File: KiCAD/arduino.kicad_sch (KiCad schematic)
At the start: 2 parts, among them U1 Si5351A_Breakout, U2 Metro_ESP32S3

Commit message: Work in Progress
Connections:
- net 3V3: now reaches U2.3V3_L (3V3)
- net 3V3: now also U1.VIN
- net SDA: now reaches U2.A4 (A4/SDA)
- net SDA: now also U1.SDA
- net SCL: now reaches U2.A5 (A5/SCL)
- net SCL: now also U1.SCL
- net GND: now reaches U2.GND_L (GND)
- net GND: now also U1.GND
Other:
- note added: "I2C pull-ups provided by Si5351A breakout (10 kΩ to 3.3 V). No additional pull-ups needed."

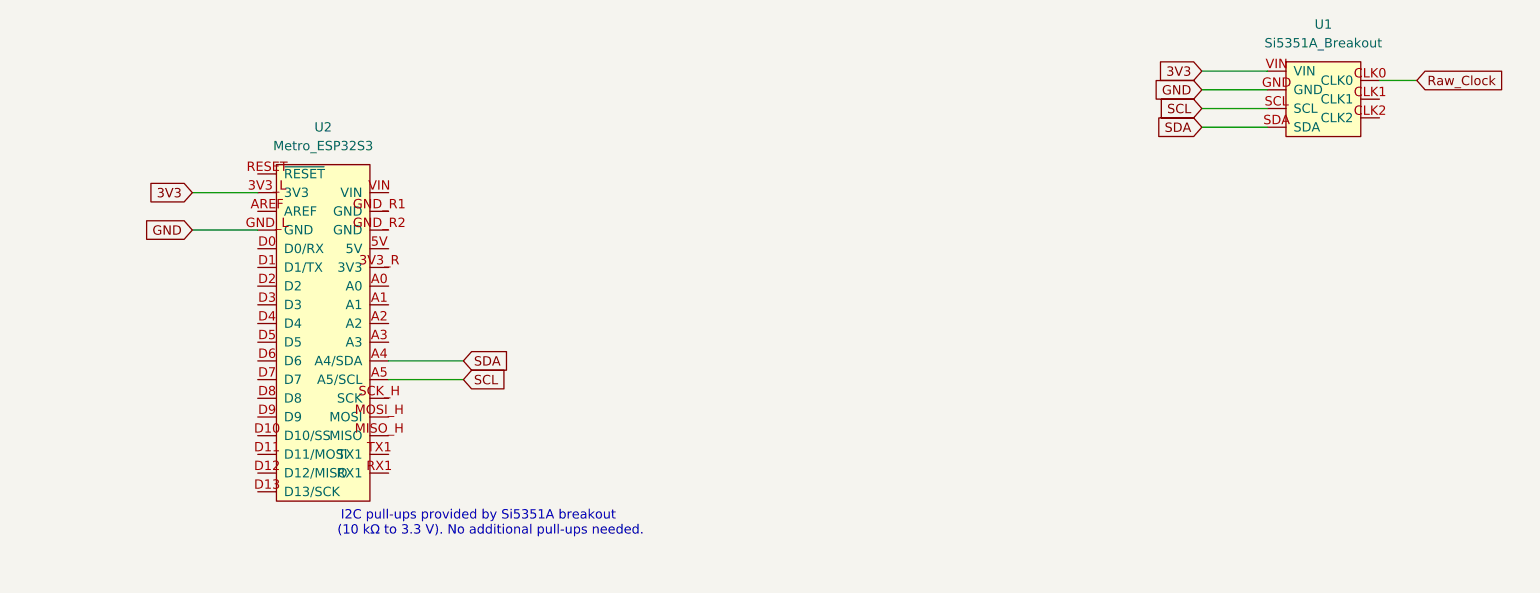
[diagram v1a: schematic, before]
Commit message: kicad: control-board sheets — buffer_keyer keyer body, arduino SPI labels, custom-symbol plan
- buffer_keyer.kicad_sch: place MC1496 keyer support components
  (carrier divider R11/R12, modulator port R3, emitter-degen Re,
  modulator coupling C1, VEE bypass C5, R2 Iee, bypass network),
  MCP4921 envelope DAC U4 with reconstruction cap C3, terminal
  blocks J1/J2/J3 for +5V/+12V/-90V/VEE input, hierarchical labels
  for VFO_OUT, SCK, MOSI, CS_DAC.
- arduino.kicad_sch: add SCK and MOSI hierarchical outputs for SPI
  link to MCP4921. CS_DAC still TODO.
- vfo.kicad_sch + KiCAD.kicad_sch: minor edits, sheet pin updates.
- Documentation/kicad_custom_symbols.md: new doc — pattern and plan
  for project-local xmitter:Metro_ESP32S3 symbol to replace the
  cluttered stock symbol (~30 pins → 10 pins, project-named).
- VFO_Keyer_Order.xlsx: small status updates.
- xmitter_prj/keyer.sch: minor cleanup.
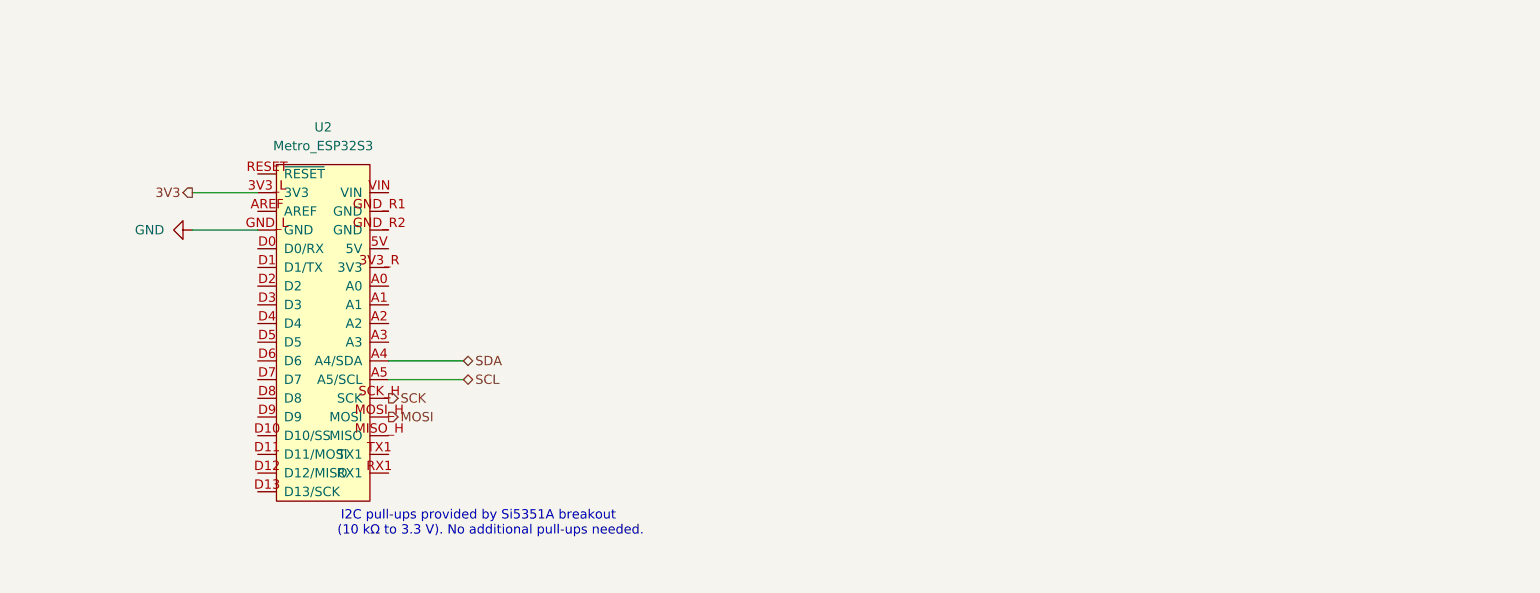
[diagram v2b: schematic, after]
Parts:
- removed U1: Si5351A_Breakout, symbol xmitter:Si5351A_Breakout
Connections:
- net MOSI: now reaches U2.MOSI_H (MOSI)
- net SCK: now reaches U2.SCK_H (SCK)

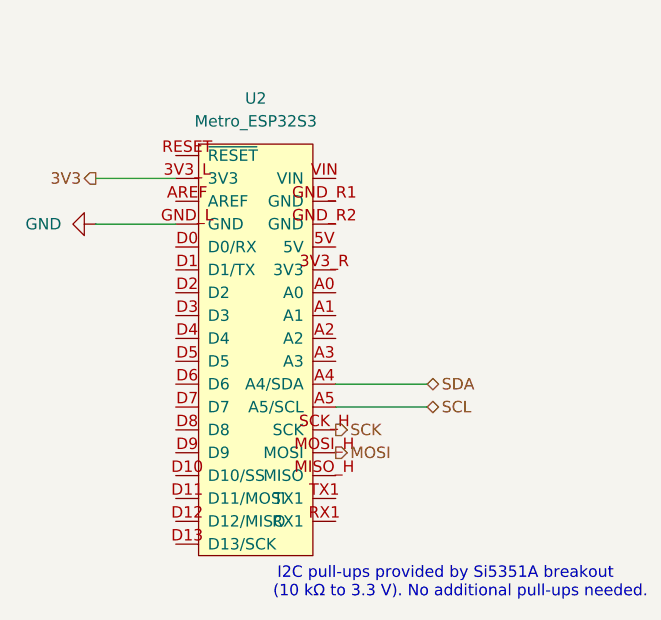
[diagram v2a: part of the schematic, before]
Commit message: kicad: redesign Metro_ESP32S3 as wide 25-pin xmitter symbol + wire arduino sheet
- xmitter.kicad_sym: replace Metro_ESP32S3 with a 25-pin compact symbol
  (was 34-pin stock with cluttered alt-function labels). Body 25.4 x
  34.3 mm. 19 active pins (power, control, UART, I2C, SPI, paddle,
  TX_LED) + 6 analog spares (A0-A5) for future expansion.
- arduino.kicad_sch: cached lib_symbols mirrors the new definition; wire
  Metro pins to hierarchical labels (SDA, SCL, SCK, MOSI, CS_DAC, 3V3)
  and to GND/+5V power ports. CS_DAC label added for SPI chip select.
- buffer_keyer.kicad_sch: keyer body wiring progress (22 wires).
- tools/rewrite_metro_symbol.py: idempotent symbol generator. Pin list
  is declarative (LEFT_PINS / RIGHT_PINS); body height auto-sizes to
  the longest column. Rewrites both the live library and the cached
  lib_symbols block in arduino.kicad_sch in one pass, with CRLF
  preserved and explicit no-BOM writes (KiCad 10 silently treats
  BOM-prefixed .kicad_sym as empty).
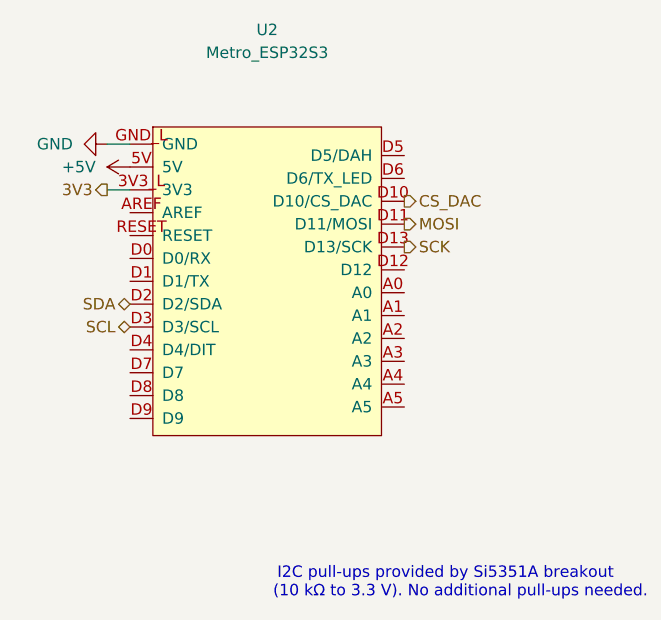
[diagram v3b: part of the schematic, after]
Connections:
- net MOSI: now also U2.D11 (D11/MOSI); no longer U2.MOSI_H (MOSI)
- net SCK: now also U2.D13 (D13/SCK); no longer U2.SCK_H (SCK)
- net SCL: now also U2.D3 (D3/SCL); no longer U2.A5 (A5/SCL)
- net SDA: now also U2.D2 (D2/SDA); no longer U2.A4 (A4/SDA)
- net +5V: now reaches U2.5V
- net CS_DAC: now reaches U2.D10 (D10/CS_DAC)
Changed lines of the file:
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@@
 	(wire
 		(pts
-			(xy 111.76 85.09) (xy 121.92 85.09)
+			(xy 86.36 58.42) (xy 88.9 58.42)
 		)
 		(stroke
@@
 	(wire
 		(pts
-			(xy 85.09 62.23) (xy 93.98 62.23)
+			(xy 86.36 63.5) (xy 88.9 63.5)
 		)
 		(stroke
@@
 		)
 	)
-	(wire
-		(pts
-			(xy 85.09 67.31) (xy 93.98 67.31)
-		)
-		(stroke
-			(width 0)
-			(type default)
-		)
-	)
-	(wire
-		(pts
-			(xy 111.76 87.63) (xy 121.92 87.63)
-		)
-		(stroke
-			(width 0)
-			(type default)
-		)
-	)
 	(hierarchical_label "SCL"
 		(shape bidirectional)
-		(at 121.92 87.63 0)
-		(effects
-			(font
-				(size 1.27 1.27)
-			)
-			(justify left)
+		(at 88.9 78.74 180)
+		(effects
+			(font
+				(size 1.27 1.27)
+			)
+			(justify right)
 		)
 	)
 	(hierarchical_label "SDA"
 		(shape bidirectional)
-		(at 121.92 85.09 0)
+		(at 88.9 76.2 180)
+		(effects
+			(font
+				(size 1.27 1.27)
+			)
+			(justify right)
+		)
+	)
+	(hierarchical_label "CS_DAC"
+		(shape output)
+		(at 119.38 64.77 0)
 		(effects
 			(font
@@
 	(hierarchical_label "SCK"
 		(shape output)
-		(at 111.76 90.17 0)
+		(at 119.38 69.85 0)
 		(effects
 			(font
@@
 	(hierarchical_label "3V3"
 		(shape output)
-		(at 85.09 62.23 180)
+		(at 86.36 63.5 180)
 		(effects
 			(font
@@
 	(hierarchical_label "MOSI"
 		(shape output)
-		(at 111.76 92.71 0)
+		(at 119.38 67.31 0)
 		(effects
 			(font
@@
 	(symbol
 		(lib_id "xmitter:Metro_ESP32S3")
-		(at 102.87 81.28 0)
+		(at 104.14 73.66 0)
 		(unit 1)
 		(body_style 1)
@@
 		(fields_autoplaced yes)
 		(property "Reference" "U2"
-			(at 102.87 53.34 0)
+			(at 104.14 45.72 0)
 			(show_name no)
 			(do_not_autoplace no)
@@
 		)
 		(property "Value" "Metro_ESP32S3"
-			(at 102.87 55.88 0)
+			(at 104.14 48.26 0)
 			(show_name no)
 			(do_not_autoplace no)
@@
 		)
 		(property "Footprint" ""
-			(at 102.87 81.28 0)
+			(at 104.14 73.66 0)
 			(hide yes)
 			(show_name no)
@@
 		)
 		(property "Datasheet" "https://learn.adafruit.com/adafruit-metro-esp32-s3"
-			(at 102.87 81.28 0)
+			(at 104.14 73.66 0)
 			(hide yes)
 			(show_name no)
@@
 		)
 		(property "Description" "Adafruit Metro ESP32-S3, Arduino-compatible module"
-			(at 102.87 81.28 0)
+			(at 104.14 73.66 0)
 			(hide yes)
 			(show_name no)
@@
 		)
 		(property "Manufacturer" "Adafruit Industries"
-			(at 102.87 81.28 0)
+			(at 104.14 73.66 0)
 			(hide yes)
 			(show_name no)
@@
 		)
 		(property "MPN" "Adafruit #5500"
-			(at 102.87 81.28 0)
+			(at 104.14 73.66 0)
 			(hide yes)
 			(show_name no)
@@
 		(pin "D12"
 		)
+		(pin "3V3_L"
+		)
+		(pin "D2"
+		)
+		(pin "A1"
+		)
+		(pin "D5"
+		)
+		(pin "D4"
+		)
+		(pin "D8"
+		)
+		(pin "A0"
+		)
+		(pin "D9"
+		)
+		(pin "D10"
+		)
+		(pin "D7"
+		)
+		(pin "D3"
+		)
+		(pin "D11"
+		)
+		(pin "D13"
+		)
+		(pin "GND_L"
+		)
+		(pin "AREF"
+		)
 		(pin "D1"
 		)
-		(pin "GND_R1"
-		)
-		(pin "3V3_L"
-		)
-		(pin "D2"
+		(pin "5V"
+		)
+		(pin "A2"
+		)
+		(pin "A3"
+		)
+		(pin "A4"
+		)
+		(pin "A5"
+		)
+		(pin "D0"
 		)
 		(pin "RESET"
-		)
-		(pin "A1"
-		)
-		(pin "A4"
-		)
-		(pin "3V3_R"
-		)
-		(pin "D5"
-		)
-		(pin "A2"
-		)
-		(pin "D4"
-		)
-		(pin "D0"
-		)
-		(pin "D8"
-		)
-		(pin "AREF"
-		)
-		(pin "A0"
-		)
-		(pin "A5"
-		)
-		(pin "D9"
-		)
-		(pin "D10"
-		)
-		(pin "D7"
-		)
-		(pin "5V"
-		)
-		(pin "D3"
-		)
-		(pin "A3"
-		)
-		(pin "D11"
-		)
-		(pin "D13"
-		)
-		(pin "GND_L"
-		)
-		(pin "GND_R2"
-		)
-		(pin "MISO_H"
-		)
-		(pin "MOSI_H"
-		)
-		(pin "SCK_H"
-		)
-		(pin "RX1"
-		)
-		(pin "TX1"
-		)
-		(pin "VIN"
 		)
 		(instances
@@
 	)
 	(symbol
+		(lib_id "power:+5V")
+		(at 88.9 60.96 90)
+		(unit 1)
+		(body_style 1)
+		(exclude_from_sim no)
+		(in_bom yes)
+		(on_board yes)
+		(in_pos_files yes)
+		(dnp no)
+		(fields_autoplaced yes)
+		(property "Reference" "#PWR030"
+			(at 92.71 60.96 0)
+			(hide yes)
+			(show_name no)
+			(do_not_autoplace no)
+			(effects
+				(font
+					(size 1.27 1.27)
+				)
+			)
+		)
+		(property "Value" "+5V"
+			(at 85.09 60.9599 90)
+			(show_name no)
+			(do_not_autoplace no)
+			(effects
+				(font
+					(size 1.27 1.27)
+				)
+				(justify left)
+			)
+		)
+		(property "Footprint" ""
+			(at 88.9 60.96 0)
+			(hide yes)
+			(show_name no)
+			(do_not_autoplace no)
+			(effects
+				(font
+					(size 1.27 1.27)
+				)
+			)
+		)
+		(property "Datasheet" ""
+			(at 88.9 60.96 0)
+			(hide yes)
+			(show_name no)
+			(do_not_autoplace no)
+			(effects
+				(font
+					(size 1.27 1.27)
+				)
+			)
+		)
+		(property "Description" "Power symbol creates a global label with name \"+5V\""
+			(at 88.9 60.96 0)
+			(hide yes)
+			(show_name no)
+			(do_not_autoplace no)
+			(effects
+				(font
+					(size 1.27 1.27)
+				)
+			)
+		)
+		(pin "1"
+		)
+		(instances
+			(project "KiCAD"
+				(path "/d3de40b8-856b-4fbd-829c-f45ffcd55742/2d83d0b5-86d4-4ced-ab68-6465e3dc2d72"
+					(reference "#PWR030")
+					(unit 1)
+				)
+			)
+		)
+	)
+	(symbol
 		(lib_id "power:GND")
-		(at 85.09 67.31 270)
+		(at 86.36 58.42 270)
 		(unit 1)
 		(body_style 1)
@@
 		(fields_autoplaced yes)
 		(property "Reference" "#PWR021"
-			(at 78.74 67.31 0)
+			(at 80.01 58.42 0)
 			(hide yes)
 			(show_name no)
@@
 		)
 		(property "Value" "GND"
-			(at 81.28 67.3099 90)
+			(at 82.55 58.4199 90)
 			(show_name no)
 			(do_not_autoplace no)
@@
 		)
 		(property "Footprint" ""
-			(at 85.09 67.31 0)
+			(at 86.36 58.42 0)
 			(hide yes)
 			(show_name no)
@@
 		)
 		(property "Datasheet" ""
-			(at 85.09 67.31 0)
+			(at 86.36 58.42 0)
 			(hide yes)
 			(show_name no)
@@
 		)
 		(property "Description" "Power symbol creates a global label with name \"GND\" , ground"
-			(at 85.09 67.31 0)
-			(hide yes)
-			(show_name no)
+			(at 86.36 58.42 0)
+			(hide yes)
+			(show_name no)

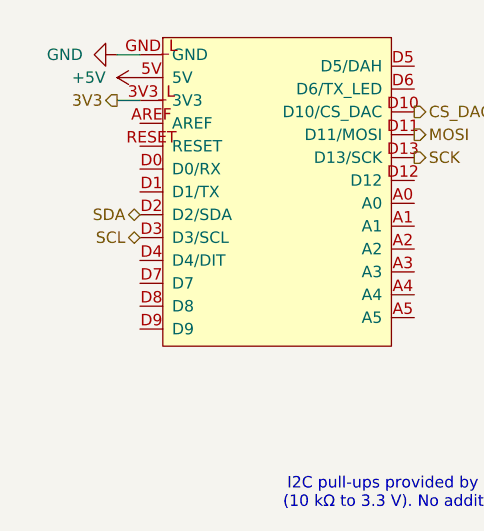
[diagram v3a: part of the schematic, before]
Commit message: docs(keyer): correct null-injection topology to match QUCS sim and MC1496 app note
The "Future enhancement: DAC-driven digital carrier null" section of
cw_envelope_keyer.md described "330 kohm direct injection at MC1496
pins 1/4 (SIG_P, SIG_N)". That description was wrong on two counts:

1. It contradicts what xmitter_prj/keyer.sch actually simulates. In the
   QUCS schematic, the DAC1/DAC2 ports tie DIRECTLY to T1/T2 PNP bases
   (with V8 = 1.65 V as the static null-test bias). The DACs were never
   wired to MC1496 pins 1/4.

2. It would violate the MC1496 application note (AN531 page 5): "Good
   carrier suppression over a wide temperature range requires low dc
   resistances between the bases of the lower differential amplifier
   (pins 1 and 4) and ground… not significantly higher than the 51 ohms
   utilized in the circuit shown in Figure 3." Adding 330 kohm to pins
   1/4 would raise that DC resistance and degrade null performance vs
   temperature.

The correct topology (matching QUCS + buffer_keyer.kicad_sch +
the app note) is PNP-base modulation: DAC -> 330 kohm -> PNP base,
which trims the existing PNP-injection nulling scheme via the
transistor's transconductance. The 51-ohm R3/R4 resistors at pins 1/4
stay in place, satisfying the app note constraint.

Other changes in this commit:
- buffer_keyer.kicad_sch / KiCAD.kicad_pro / arduino.kicad_sch: minor
  edits made during the deep-dive session.
- tools/trace_buffer_keyer_nets.py + tools/trace_specific_nets.py: net
  tracer scripts written during the deep-dive (extract chip pin
  connectivity, find floating pins, verify topology against QUCS).
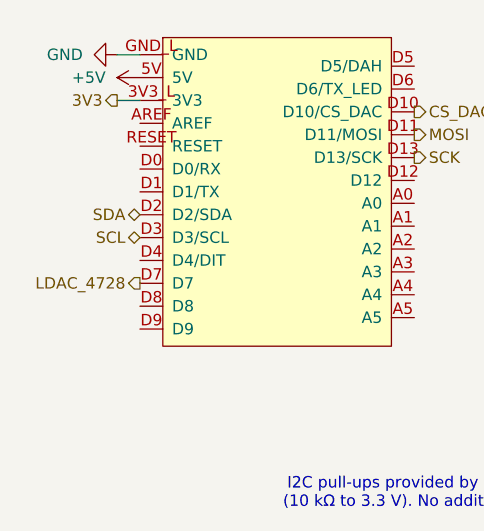
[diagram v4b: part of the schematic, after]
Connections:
- net LDAC_4728: now reaches U2.D7
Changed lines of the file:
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@@
+		)
+	)
+	(hierarchical_label "LDAC_4728"
+		(shape output)
+		(at 88.9 83.82 180)
+		(effects
+			(font
+				(size 1.27 1.27)
+			)
+			(justify right)
 		)
 	)
